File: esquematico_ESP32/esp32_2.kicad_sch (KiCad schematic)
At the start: 9 parts, among them SW1 SW_Push, SW2 Enable, U1 ESP32-WROOM-32

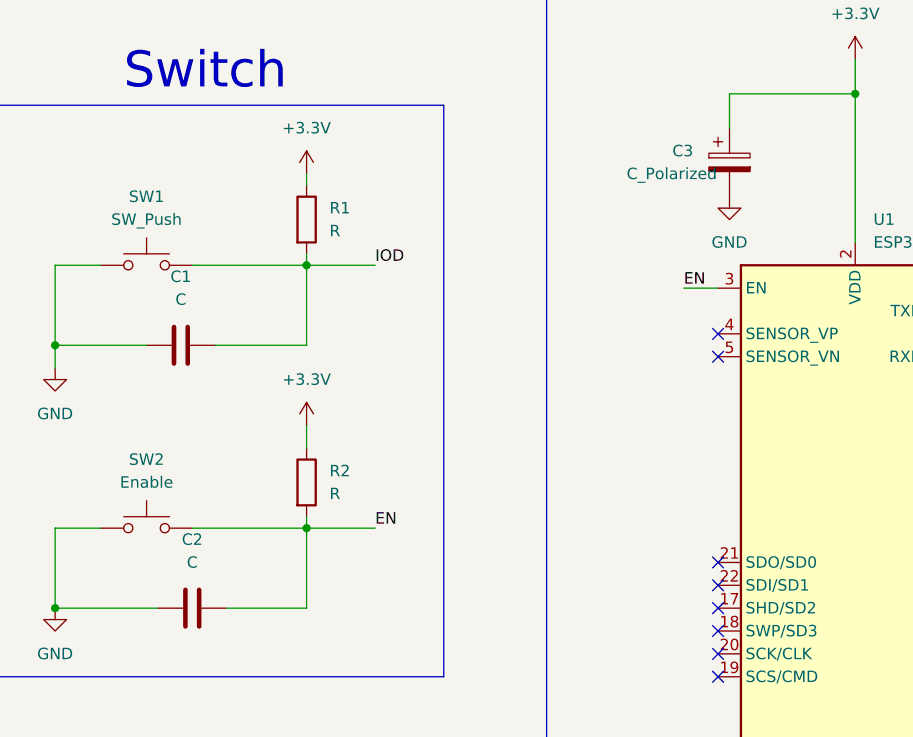
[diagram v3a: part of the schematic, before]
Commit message: se agregaron los valores (pendiente última revisión)
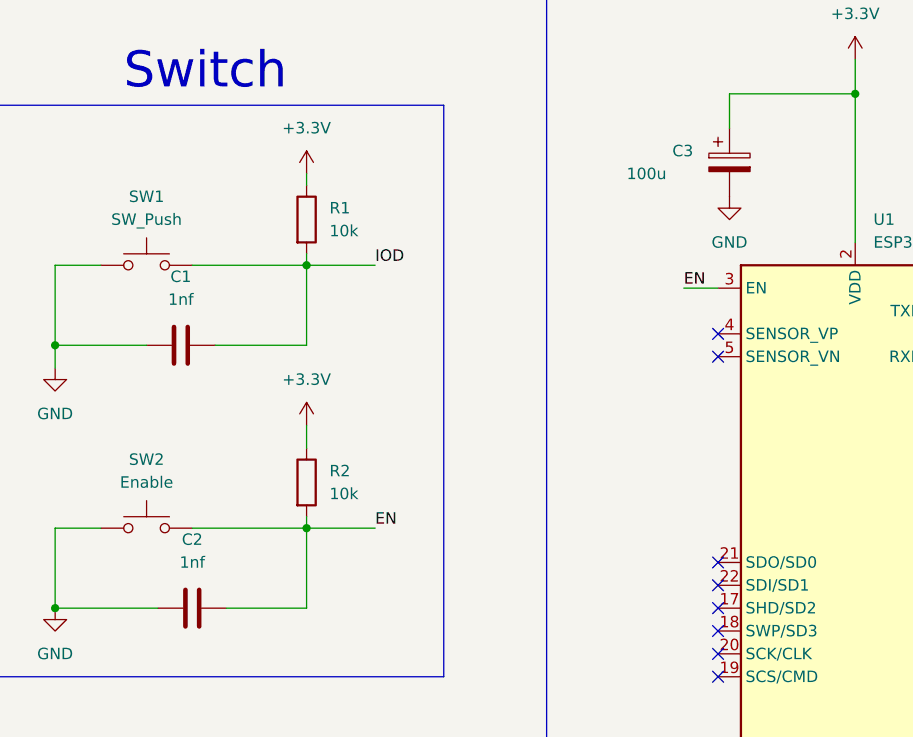
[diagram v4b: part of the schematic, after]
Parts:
- C1, C2: value C -> 1nf
- C3: value C_Polarized -> 100u
- R1, R2: value R -> 10k
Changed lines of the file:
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@@
       (effects (font (size 1.27 1.27)) (justify left))
     )
-    (property "Value" "C_Polarized" (id 1) (at 195.58 46.99 0)
+    (property "Value" "100u" (id 1) (at 195.58 46.99 0)
       (effects (font (size 1.27 1.27)) (justify left))
     )
@@
       (effects (font (size 1.27 1.27)) (justify left))
     )
-    (property "Value" "R" (id 1) (at 162.56 53.3399 0)
+    (property "Value" "10k" (id 1) (at 162.56 53.3399 0)
       (effects (font (size 1.27 1.27)) (justify left))
     )
@@
     (in_bom yes) (on_board yes) (fields_autoplaced)
     (property "Reference" "C1" (id 0) (at 146.05 58.42 90))
-    (property "Value" "C" (id 1) (at 146.05 60.96 90))
+    (property "Value" "1nf" (id 1) (at 146.05 60.96 90))
     (property "Footprint" "Capacitor_SMD:C_0805_2012Metric_Pad1.18x1.45mm_HandSolder" (id 2) (at 149.86 65.0748 0)
       (effects (font (size 1.27 1.27)) hide)
@@
     (in_bom yes) (on_board yes)
     (property "Reference" "C2" (id 0) (at 147.32 87.63 90))
-    (property "Value" "C" (id 1) (at 147.32 90.17 90))
+    (property "Value" "1nf" (id 1) (at 147.32 90.17 90))
     (property "Footprint" "Capacitor_SMD:C_0805_2012Metric_Pad1.18x1.45mm_HandSolder" (id 2) (at 151.13 94.2848 0)
       (effects (font (size 1.27 1.27)) hide)
@@
       (effects (font (size 1.27 1.27)) (justify left))
     )
-    (property "Value" "R" (id 1) (at 162.56 82.5499 0)
+    (property "Value" "10k" (id 1) (at 162.56 82.5499 0)
       (effects (font (size 1.27 1.27)) (justify left))
     )
@@
     )
     (path "/c68781dd-0297-4f6e-84e0-25d6f076977b"
-      (reference "C1") (unit 1) (value "C") (footprint "Capacitor_SMD:C_0805_2012Metric_Pad1.18x1.45mm_HandSolder")
+      (reference "C1") (unit 1) (value "1nf") (footprint "Capacitor_SMD:C_0805_2012Metric_Pad1.18x1.45mm_HandSolder")
     )
     (path "/efd3296c-45d0-4644-8ca7-86a2b5d08997"
-      (reference "C2") (unit 1) (value "C") (footprint "Capacitor_SMD:C_0805_2012Metric_Pad1.18x1.45mm_HandSolder")
+      (reference "C2") (unit 1) (value "1nf") (footprint "Capacitor_SMD:C_0805_2012Metric_Pad1.18x1.45mm_HandSolder")
     )
     (path "/0a8fb98b-26c6-43af-94b5-0a498a75c195"
-      (reference "C3") (unit 1) (value "C_Polarized") (footprint "Capacitor_SMD:C_0805_2012Metric_Pad1.18x1.45mm_HandSolder")
+      (reference "C3") (unit 1) (value "100u") (footprint "Capacitor_SMD:C_0805_2012Metric_Pad1.18x1.45mm_HandSolder")
     )
     (path "/5125aeff-fbaf-4069-9b26-eba443c92f10/47a92999-85b6-4838-bf9c-de8805710a0e"
-      (reference "C4") (unit 1) (value "C") (footprint "Capacitor_SMD:C_0805_2012Metric_Pad1.18x1.45mm_HandSolder")
+      (reference "C4") (unit 1) (value "100n") (footprint "Capacitor_SMD:C_0805_2012Metric_Pad1.18x1.45mm_HandSolder")
     )
     (path "/5125aeff-fbaf-4069-9b26-eba443c92f10/cd914efc-af8e-4f0a-a357-7058f3b85b01"
-      (reference "C5") (unit 1) (value "C") (footprint "Capacitor_SMD:C_0805_2012Metric_Pad1.18x1.45mm_HandSolder")
+      (reference "C5") (unit 1) (value "10u") (footprint "Capacitor_SMD:C_0805_2012Metric_Pad1.18x1.45mm_HandSolder")
     )
     (path "/5125aeff-fbaf-4069-9b26-eba443c92f10/e5762204-9e07-48f8-b103-f84e0a819e65"
-      (reference "C6") (unit 1) (value "C") (footprint "Capacitor_SMD:C_0805_2012Metric_Pad1.18x1.45mm_HandSolder")
+      (reference "C6") (unit 1) (value "22u") (footprint "Capacitor_SMD:C_0805_2012Metric_Pad1.18x1.45mm_HandSolder")
     )
     (path "/5125aeff-fbaf-4069-9b26-eba443c92f10/2433beca-5958-4b6f-9211-d9011a22816b"
-      (reference "C7") (unit 1) (value "C") (footprint "Capacitor_SMD:C_0805_2012Metric_Pad1.18x1.45mm_HandSolder")
+      (reference "C7") (unit 1) (value "100n") (footprint "Capacitor_SMD:C_0805_2012Metric_Pad1.18x1.45mm_HandSolder")
     )
     (path "/5125aeff-fbaf-4069-9b26-eba443c92f10/ab816942-ca37-4395-8381-87b62ed341fa/dcc85525-25f6-4689-aa85-18b1b3f46250"
-      (reference "C8") (unit 1) (value "C_Polarized") (footprint "Capacitor_SMD:CP_Elec_8x6.9")
+      (reference "C8") (unit 1) (value "470u") (footprint "Capacitor_SMD:CP_Elec_8x6.9")
     )
     (path "/5125aeff-fbaf-4069-9b26-eba443c92f10/ab816942-ca37-4395-8381-87b62ed341fa/c668d07b-48e5-47c8-9250-6d6fb4e7607d"
-      (reference "C9") (unit 1) (value "C") (footprint "Capacitor_SMD:C_0805_2012Metric_Pad1.18x1.45mm_HandSolder")
+      (reference "C9") (unit 1) (value "1n") (footprint "Capacitor_SMD:C_0805_2012Metric_Pad1.18x1.45mm_HandSolder")
     )
     (path "/5125aeff-fbaf-4069-9b26-eba443c92f10/ab816942-ca37-4395-8381-87b62ed341fa/6adfb656-fadb-4782-8076-f8717b94ce86"
-      (reference "C10") (unit 1) (value "C_Polarized") (footprint "Capacitor_SMD:CP_Elec_8x6.9")
+      (reference "C10") (unit 1) (value "220u") (footprint "Capacitor_SMD:CP_Elec_8x6.9")
     )
     (path "/90dc18a7-d136-49c5-aca7-9f578dd2dde7/7cbb4cf2-d39b-4cae-b2fd-23730c35b330"
@@
     )
     (path "/5125aeff-fbaf-4069-9b26-eba443c92f10/ab816942-ca37-4395-8381-87b62ed341fa/98c852c7-4008-4e0f-89ac-3d2c8aa0e3a2"
-      (reference "D4") (unit 1) (value "DIODE") (footprint "Diode_THT:D_DO-27_P12.70mm_Horizontal")
+      (reference "D4") (unit 1) (value "1N5819") (footprint "Diode_THT:D_DO-27_P12.70mm_Horizontal")
     )
     (path "/90dc18a7-d136-49c5-aca7-9f578dd2dde7/871fe201-8570-4ab4-b58c-0d248a209c25"
@@
     )
     (path "/5125aeff-fbaf-4069-9b26-eba443c92f10/ab816942-ca37-4395-8381-87b62ed341fa/1c0db303-6554-463d-b3e6-31f60af3b913"
-      (reference "L1") (unit 1) (value "L") (footprint "Inductor_SMD:L_Neosid_SM-PIC0612H")
+      (reference "L1") (unit 1) (value "47u") (footprint "Inductor_SMD:L_Neosid_SM-PIC0612H")
     )
     (path "/5b1134d1-ab5f-48fa-b527-ffdc1b4c5ff5"
@@
     )
     (path "/811fc961-3b53-4988-9d52-c2af6da587e1"
-      (reference "R1") (unit 1) (value "R") (footprint "Resistor_SMD:R_0805_2012Metric_Pad1.20x1.40mm_HandSolder")
+      (reference "R1") (unit 1) (value "10k") (footprint "Resistor_SMD:R_0805_2012Metric_Pad1.20x1.40mm_HandSolder")
     )
     (path "/f0f39cd4-ec10-4740-8c9f-2a648fe1ba10"
-      (reference "R2") (unit 1) (value "R") (footprint "Resistor_SMD:R_0805_2012Metric_Pad1.20x1.40mm_HandSolder")
+      (reference "R2") (unit 1) (value "10k") (footprint "Resistor_SMD:R_0805_2012Metric_Pad1.20x1.40mm_HandSolder")
     )
     (path "/90dc18a7-d136-49c5-aca7-9f578dd2dde7/996ed483-6936-4c87-b966-27267e8b6020"
-      (reference "R3") (unit 1) (value "R") (footprint "Resistor_SMD:R_0805_2012Metric_Pad1.20x1.40mm_HandSolder")
+      (reference "R3") (unit 1) (value "10k") (footprint "Resistor_SMD:R_0805_2012Metric_Pad1.20x1.40mm_HandSolder")
     )
     (path "/90dc18a7-d136-49c5-aca7-9f578dd2dde7/8c3aef16-78ad-446d-98dc-ff48ffd791f4"
-      (reference "R4") (unit 1) (value "R") (footprint "Resistor_SMD:R_0805_2012Metric_Pad1.20x1.40mm_HandSolder")
+      (reference "R4") (unit 1) (value "10k") (footprint "Resistor_SMD:R_0805_2012Metric_Pad1.20x1.40mm_HandSolder")
     )
     (path "/5125aeff-fbaf-4069-9b26-eba443c92f10/d9d51edd-1153-42e2-964d-e921c035d9b5"
-      (reference "R5") (unit 1) (value "R") (footprint "Resistor_SMD:R_0805_2012Metric_Pad1.20x1.40mm_HandSolder")
+      (reference "R5") (unit 1) (value "10k") (footprint "Resistor_SMD:R_0805_2012Metric_Pad1.20x1.40mm_HandSolder")
     )
     (path "/90dc18a7-d136-49c5-aca7-9f578dd2dde7/f793cc0c-ede8-43dc-9a01-a81d5ad3f9fc/089b9fe9-7f92-4a3b-aa42-3337ce56dfc4"
-      (reference "R6") (unit 1) (value "R") (footprint "Resistor_SMD:R_0805_2012Metric_Pad1.20x1.40mm_HandSolder")
+      (reference "R6") (unit 1) (value "10k") (footprint "Resistor_SMD:R_0805_2012Metric_Pad1.20x1.40mm_HandSolder")
     )
     (path "/90dc18a7-d136-49c5-aca7-9f578dd2dde7/f793cc0c-ede8-43dc-9a01-a81d5ad3f9fc/7f3bd6e5-4984-4745-b8cc-78bf883eceac"
-      (reference "R7") (unit 1) (value "R") (footprint "Resistor_SMD:R_0805_2012Metric_Pad1.20x1.40mm_HandSolder")
+      (reference "R7") (unit 1) (value "10k") (footprint "Resistor_SMD:R_0805_2012Metric_Pad1.20x1.40mm_HandSolder")
     )
     (path "/90dc18a7-d136-49c5-aca7-9f578dd2dde7/f793cc0c-ede8-43dc-9a01-a81d5ad3f9fc/fa1fb6b7-c8b0-45dc-ae6b-5d84c42178db"
-      (reference "R8") (unit 1) (value "R") (footprint "Resistor_SMD:R_0805_2012Metric_Pad1.20x1.40mm_HandSolder")
+      (reference "R8") (unit 1) (value "10k") (footprint "Resistor_SMD:R_0805_2012Metric_Pad1.20x1.40mm_HandSolder")
     )
     (path "/90dc18a7-d136-49c5-aca7-9f578dd2dde7/f793cc0c-ede8-43dc-9a01-a81d5ad3f9fc/e47dfee4-8586-43a0-90c3-51066d051b92"
-      (reference "R9") (unit 1) (value "R") (footprint "Resistor_SMD:R_0805_2012Metric_Pad1.20x1.40mm_HandSolder")
+      (reference "R9") (unit 1) (value "10k") (footprint "Resistor_SMD:R_0805_2012Metric_Pad1.20x1.40mm_HandSolder")
     )
     (path "/5125aeff-fbaf-4069-9b26-eba443c92f10/ab816942-ca37-4395-8381-87b62ed341fa/20a047cd-7607-4abb-a367-5edb6bce472b"
-      (reference "R10") (unit 1) (value "R") (footprint "Resistor_SMD:R_0805_2012Metric_Pad1.20x1.40mm_HandSolder")
+      (reference "R10") (unit 1) (value "1k") (footprint "Resistor_SMD:R_0805_2012Metric_Pad1.20x1.40mm_HandSolder")
     )
     (path "/5125aeff-fbaf-4069-9b26-eba443c92f10/ab816942-ca37-4395-8381-87b62ed341fa/8b86c6a7-d232-4471-a423-8884526eae2e"
-      (reference "R11") (unit 1) (value "R") (footprint "Resistor_SMD:R_0805_2012Metric_Pad1.20x1.40mm_HandSolder")
+      (reference "R11") (unit 1) (value "560") (footprint "Resistor_SMD:R_0805_2012Metric_Pad1.20x1.40mm_HandSolder")
     )
     (path "/68435389-e911-43d9-accd-f38462c79cab"

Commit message: Correciones de la clase
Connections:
- net +3V3: now also Programador1.5 (Pin_5)
- net +5V: no longer names the net of Programador1.1 (Pin_1)
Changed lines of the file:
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@@
   (junction (at 132.08 66.04) (diameter 0) (color 0 0 0 0)
   )
-  (no_connect (at 264.16 67.31))
   (no_connect (at 205.74 64.77))
   (no_connect (at 205.74 67.31))
@@
   (no_connect (at 205.74 97.79))
   (no_connect (at 205.74 100.33))
+  (no_connect (at 264.16 57.15))
   (no_connect (at 236.22 80.01))
   (no_connect (at 236.22 77.47))
@@
     )
     (property "Datasheet" "" (id 3) (at 160.02 46.99 0)
+      (effects (font (size 1.27 1.27)) hide)
+    )
+    (pin "1")
+  )
+  (symbol (lib_id "power:+3.3V") (at 264.16 67.31 90) (unit 1)
+    (in_bom yes) (on_board yes)
+    (property "Reference" "#PWR0104" (id 0) (at 267.97 67.31 0)
+      (effects (font (size 1.27 1.27)) hide)
+    )
+    (property "Value" "+3.3V" (id 1) (at 261.62 69.215 90)
+      (effects (font (size 1.27 1.27)) (justify right))
+    )
+    (property "Footprint" "" (id 2) (at 264.16 67.31 0)
+      (effects (font (size 1.27 1.27)) hide)
+    )
+    (property "Datasheet" "" (id 3) (at 264.16 67.31 0)
       (effects (font (size 1.27 1.27)) hide)
     )
@@
     )
     (property "Datasheet" "" (id 3) (at 264.16 59.69 0)
-      (effects (font (size 1.27 1.27)) hide)
-    )
-    (pin "1")
-  )
-  (symbol (lib_id "power:+5V") (at 264.16 57.15 90) (unit 1)
-    (in_bom yes) (on_board yes) (fields_autoplaced)
-    (property "Reference" "#PWR016" (id 0) (at 267.97 57.15 0)
-      (effects (font (size 1.27 1.27)) hide)
-    )
-    (property "Value" "+5V" (id 1) (at 260.35 57.1499 90)
-      (effects (font (size 1.27 1.27)) (justify left))
-    )
-    (property "Footprint" "" (id 2) (at 264.16 57.15 0)
-      (effects (font (size 1.27 1.27)) hide)
-    )
-    (property "Datasheet" "" (id 3) (at 264.16 57.15 0)
       (effects (font (size 1.27 1.27)) hide)
     )
@@
       (reference "#PWR015") (unit 1) (value "GND") (footprint "")
     )
-    (path "/ec8a206d-51d0-4b19-ba1c-de1123777a8c"
-      (reference "#PWR016") (unit 1) (value "+5V") (footprint "")
-    )
     (path "/e2ad1c6b-bcd4-4f7f-9fda-ff086ea46df4"
       (reference "#PWR017") (unit 1) (value "GND") (footprint "")
@@
       (reference "#PWR0103") (unit 1) (value "+5V") (footprint "")
     )
+    (path "/163963d5-9627-43e4-ac5c-e10ad7299143"
+      (reference "#PWR0104") (unit 1) (value "+3.3V") (footprint "")
+    )
+    (path "/5125aeff-fbaf-4069-9b26-eba443c92f10/b2fca1fc-8d55-4658-8721-548fa4e11835"
+      (reference "#PWR0105") (unit 1) (value "+5V") (footprint "")
+    )
+    (path "/5125aeff-fbaf-4069-9b26-eba443c92f10/19ae38b6-aa07-4b33-9ede-24b784548caa"
+      (reference "#PWR0106") (unit 1) (value "+3.3V") (footprint "")
+    )
+    (path "/5125aeff-fbaf-4069-9b26-eba443c92f10/519b1c4e-ac36-4cc7-ad50-ac716ddb4e04"
+      (reference "#PWR0107") (unit 1) (value "GND") (footprint "")
+    )
     (path "/c68781dd-0297-4f6e-84e0-25d6f076977b"
       (reference "C1") (unit 1) (value "1nf") (footprint "Capacitor_SMD:C_0805_2012Metric_Pad1.18x1.45mm_HandSolder")
@@
       (reference "U3") (unit 1) (value "LM2596S-5") (footprint "Package_TO_SOT_SMD:TO-263-5_TabPin3")
     )
-  )
+    (path "/5125aeff-fbaf-4069-9b26-eba443c92f10/b33c26e5-c2b9-4aac-b911-133539770d9a"
+      (reference "verificación1") (unit 1) (value "Conn_01x03_Male") (footprint "Connector_PinHeader_2.54mm:PinHeader_1x03_P2.54mm_Vertical")
+    )
+  )
